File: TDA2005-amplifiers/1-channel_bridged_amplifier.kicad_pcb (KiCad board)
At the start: 2 copper layers, 19 parts, among them U1 TDA2005

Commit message: kicad6
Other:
- net class Default removed

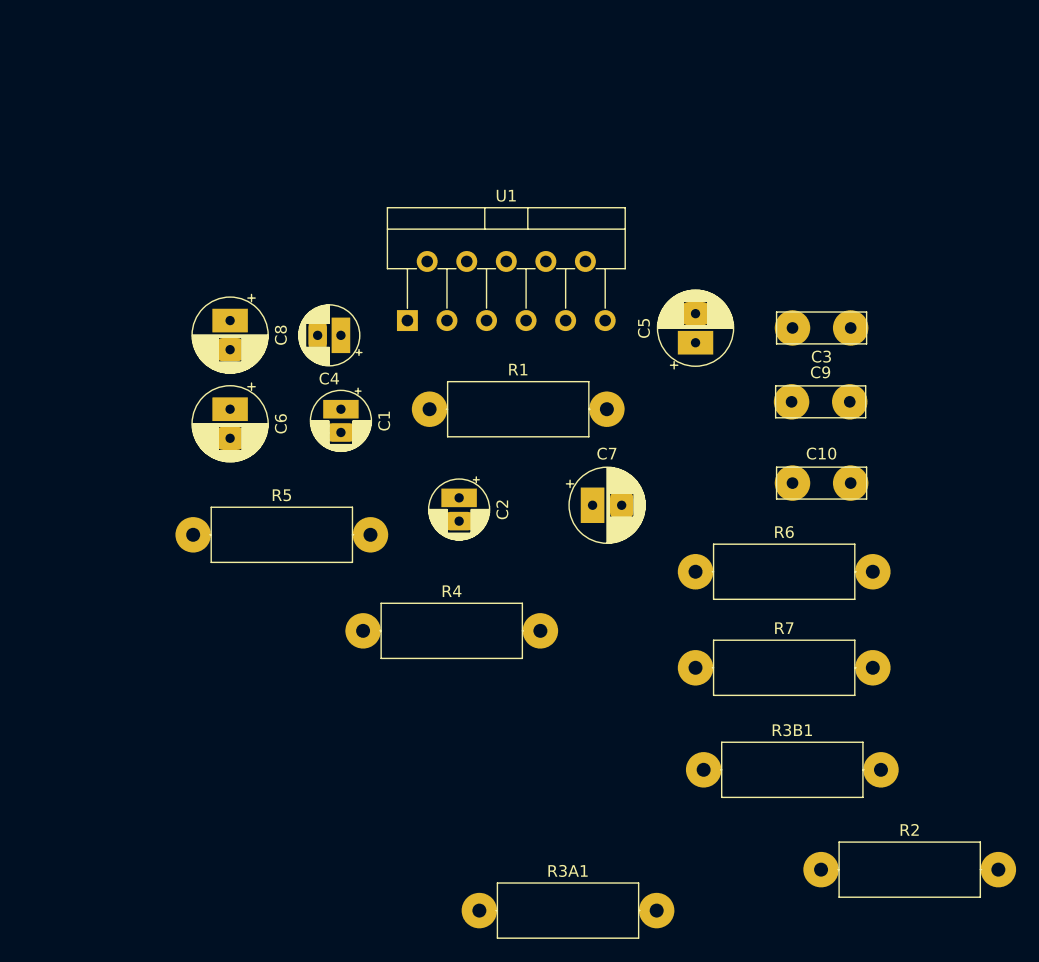
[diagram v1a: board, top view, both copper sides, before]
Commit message: bridged amplifier
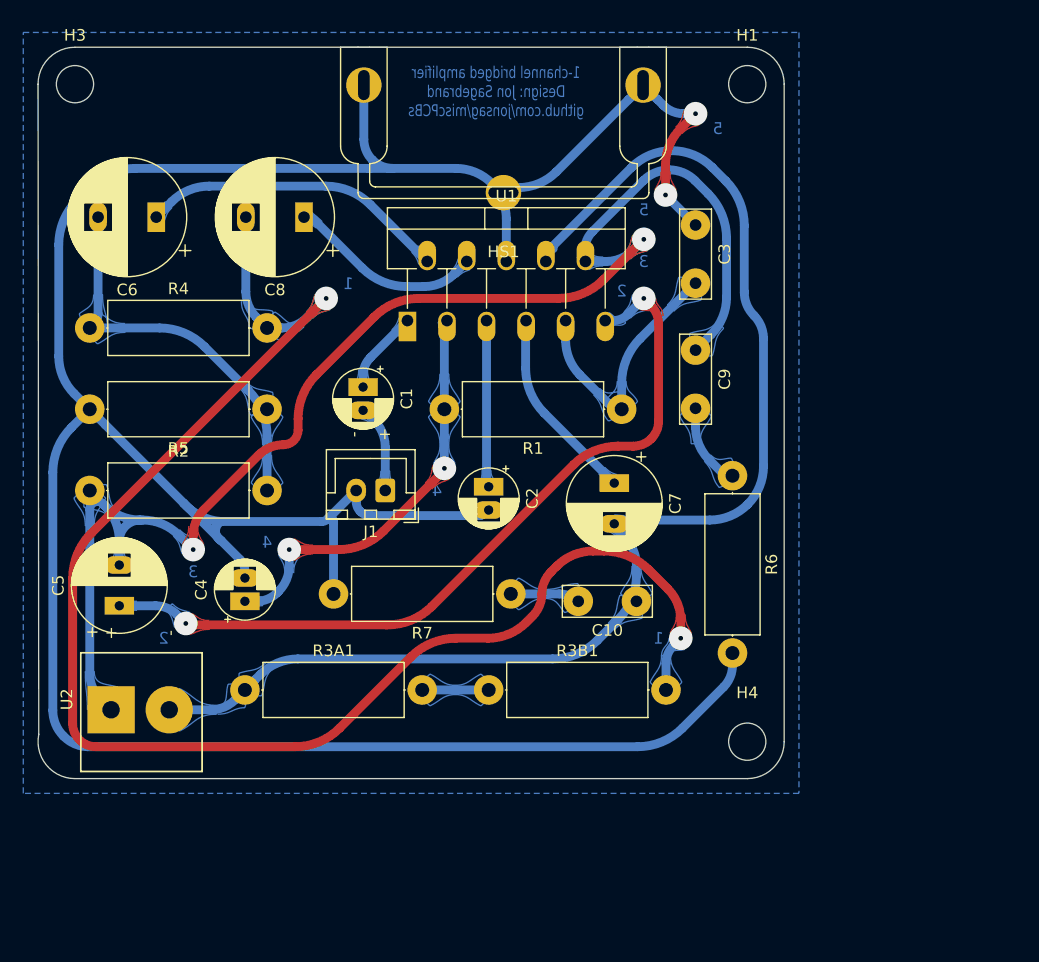
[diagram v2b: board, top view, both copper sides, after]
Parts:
- added H1: MountingHole, MountingHole:MountingHole_3.2mm_M3, F.Cu at (149.9, 48.3)
- added H3: MountingHole, MountingHole:MountingHole_3.2mm_M3, F.Cu at (92.1, 48.3)
- added H4: MountingHole, MountingHole:MountingHole_3.2mm_M3, F.Cu at (149.9, 104.8)
- added HS1: Heatsink_Pad, My_Heatsinks:EK-41002859, F.Cu at (128.9, 57.6)
- added J1: Audio In, My_Headers:2-pin JST Audio, F.Cu at (118.7, 83.2)
- added U2: Speaker Out, My_Parts:2-pole_power_in_screw_terminal, F.Cu at (95.2, 102.0)
- C5, C7: footprint My_Misc:CP_Radial_D6.3mm_P2.50mm_large -> My_Misc:CP_Radial_D8.0mm_P3.50mm_large
- C6, C8: footprint My_Misc:CP_Radial_D6.3mm_P2.50mm_large -> My_Misc:CP_Radial_D10.0mm_P5.00mm_larger
- U1: footprint Package_TO_SOT_THT:TO-220-11_P3.4x5.08mm_StaggerOdd_Lead4.85mm_Vertical -> My_Misc:TO-220-11_P3.4x5.08mm_StaggerOdd_Lead4.85mm_Vertical_large
- moved R2 70.8 mm to (93.3, 83.2)
- moved C5 54.4 mm to (95.9, 93.1)
- moved R4 35.1 mm to (93.3, 69.2)
- moved R3A1 27.7 mm to (106.7, 100.3)
- moved C4 24.3 mm to (106.7, 92.7), turned to 90 degrees
- moved R3B1 19.7 mm to (127.6, 100.3)
- moved C6 17.7 mm to (99.1, 59.7), turned to 180 degrees
- moved R7 17.1 mm to (129.5, 92.1), turned to 180 degrees
- moved C10 16.8 mm to (140.3, 92.7), turned to 180 degrees
- moved R1 16.5 mm to (139.1, 76.2), turned to 180 degrees
- moved C3 16.0 mm to (145.4, 60.4), turned to -90 degrees
- moved R5 12.5 mm to (108.6, 76.2), turned to 180 degrees
- moved C8 10.9 mm to (111.8, 59.7), turned to 180 degrees
- moved C9 9.38 mm to (145.4, 71.1), turned to -90 degrees
- moved R6 8.84 mm to (148.6, 81.9), turned to -90 degrees
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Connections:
- net In- renamed GND
- net Out+ renamed Net-(C5-Pad2)
- net Out- renamed Net-(C10-Pad1)
- C1 pad 2: In+ -> Net-(C1-Pad2)
- C6 pad 1: Net-(C6-Pad1) -> Net-(U1-Pad2)
- C6 pad 2: Net-(C6-Pad2) -> Net-(R2-Pad2)
- C8 pad 1: Net-(C8-Pad1) -> Net-(U1-Pad4)
- C8 pad 2: Net-(C8-Pad2) -> Net-(R3B1-Pad2)
- R2 pad 2: Net-(C6-Pad1) -> Net-(R2-Pad2)
- R3B1 pad 2: Net-(C8-Pad1) -> Net-(R3B1-Pad2)
- R4 pad 1: Net-(C6-Pad1) -> Net-(R2-Pad2)
- R4 pad 2: Net-(C8-Pad1) -> Net-(R3B1-Pad2)
- R5 pad 1: Net-(C6-Pad1) -> Net-(R2-Pad2)
- U1 pad 2: Net-(C6-Pad2) -> Net-(U1-Pad2)
- U1 pad 4: Net-(C8-Pad2) -> Net-(U1-Pad4)
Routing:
- net GND: track 0.00 -> 255.5 mm, vias 0 -> 2
- net Net-(R3B1-Pad2): track 0.00 -> 131.0 mm, vias 0 -> 2
- net Net-(C5-Pad2): track 0.00 -> 124.4 mm, vias 0 -> 2
- net Net-(C10-Pad1): track 0.00 -> 112.8 mm
- net Net-(U1-Pad11): track 0.00 -> 68.9 mm, vias 0 -> 2
- net Net-(R1-Pad2): track 0.00 -> 35.8 mm, vias 0 -> 2
- net Net-(R2-Pad2): track 0.00 -> 33.8 mm
- net Net-(U1-Pad2): track 0.00 -> 26.6 mm
- net +15V: track 0.00 -> 22.1 mm
- net Net-(U1-Pad4): track 0.00 -> 16.9 mm
- net Net-(U1-Pad7): track 0.00 -> 16.9 mm
- net Net-(U1-Pad5): track 0.00 -> 14.5 mm
- net Net-(C1-Pad2): track 0.00 -> 7.62 mm
- net Net-(C9-Pad2): track 0.00 -> 7.56 mm
- net Net-(U1-Pad1): track 0.00 -> 7.03 mm
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- added copper zone on B.Cu, net GND
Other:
- board outline added: 64.1 x 62.9 mm
- board text added: "1"
- board text added: "1-channel bridged amplifier Design: Jon Sagebrand github.com/jonsag/miscPCBs"
- board text added: "2"
- board text added: "3"
- board text added: "4"
- board text added: "5"
